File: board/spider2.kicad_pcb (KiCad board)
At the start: 2 copper layers, 137 x 72.5 mm, 143 parts, among them J1 NRJ6HH, J10 PJ-320A, J11 PJ359, J12 PJ359, J13 PJ359, J14 PJ359, J15 PJ359, J16 PJ359, J17 A, J19 PJ359, J2 NRJ6HH, J20 PJ359, J3 PJ359, J4 PJ359, J5 PJ359, J6 PJ-320A, J7 PJ359, J8 PJ359, J9 PJ359, P1 USB4085, Q1 AOI4286, Q2 BC547, Q3 BC547, SW2 200MDP1T2B2M2, SW3 200MDP1T2B2M2, SW4 200MDP3T1B1M6QE, U2 AP63203, U4 NE5532, U5 MAX4062, U6 MAX4062, U7 PAM8406D

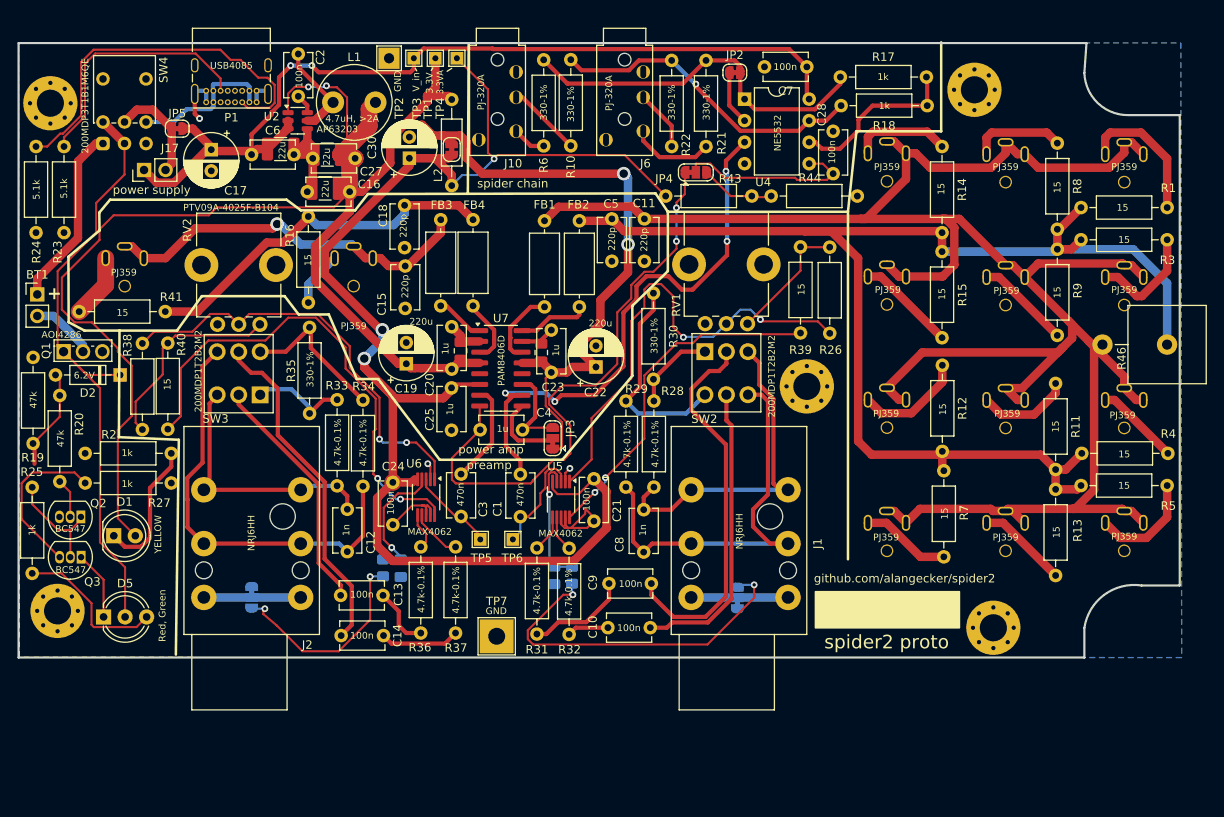
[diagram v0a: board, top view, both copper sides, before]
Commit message: option for poti inversion and some missing connections
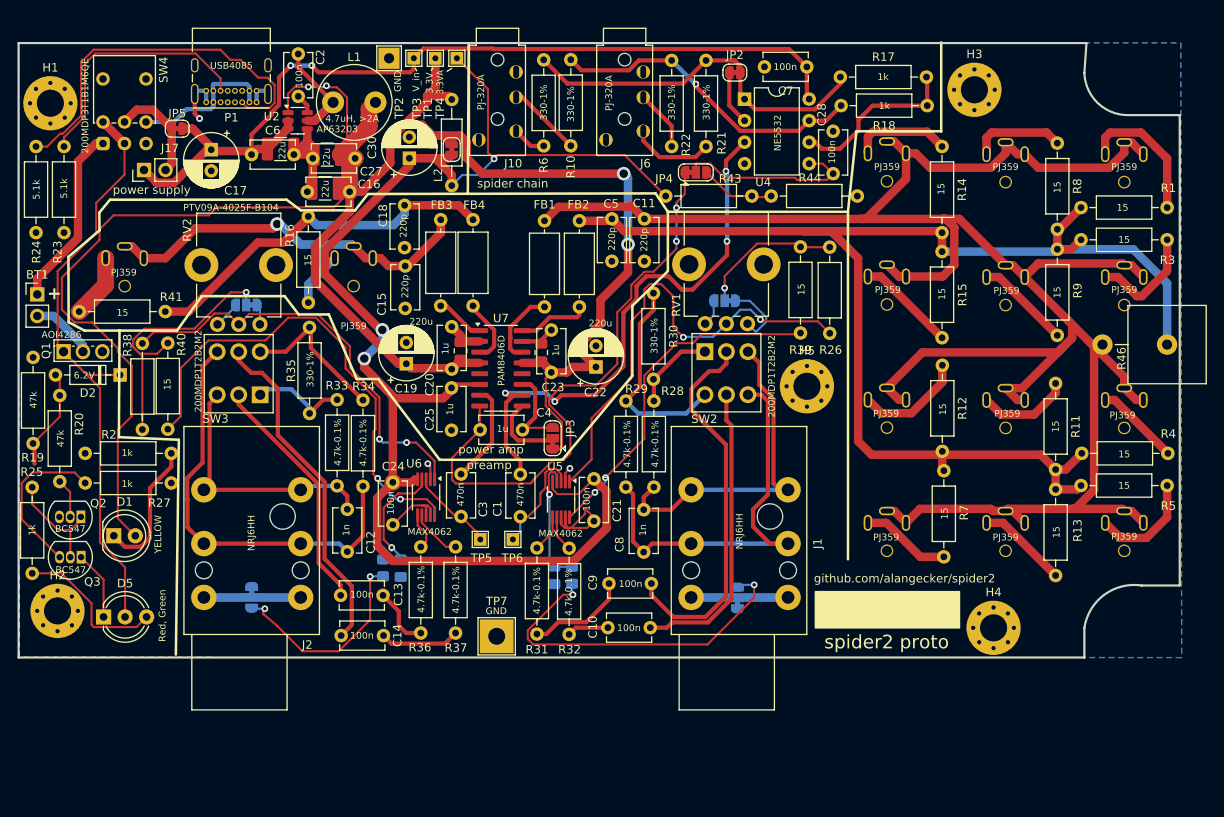
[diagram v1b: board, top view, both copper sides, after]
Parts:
- removed REF** (x5): MountingHole_3.2mm_M3_Pad_Via, MountingHole:MountingHole_3.2mm_M3_Pad_Via
- added H1: ~, MountingHole:MountingHole_3.2mm_M3_Pad_Via, F.Cu at (141.4, 37.7)
- added H2: ~, MountingHole:MountingHole_3.2mm_M3_Pad_Via, F.Cu at (142.2, 97.6)
- added H3: ~, MountingHole:MountingHole_3.2mm_M3_Pad_Via, F.Cu at (250.4, 36.1)
- added H4: ~, MountingHole:MountingHole_3.2mm_M3_Pad_Via, F.Cu at (252.7, 99.6)
- added H5: ~, MountingHole:MountingHole_3.2mm_M3_Pad_Via, F.Cu at (230.7, 71.1)
- added JP8: SolderJumper_3_Bridged12, Jumper:SolderJumper-3_P1.3mm_Bridged12_RoundedPad1.0x1.5mm, B.Cu at (220.9, 61.0)
- added JP9: SolderJumper_3_Bridged12, Jumper:SolderJumper-3_P1.3mm_Bridged12_RoundedPad1.0x1.5mm, B.Cu at (164.5, 61.5)
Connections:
- R26 pad 1: Net-(R26-Pad1) -> Net-(JP8-C)
- R38 pad 1: Net-(R38-Pad1) -> Net-(JP9-C)
- R39 pad 2: Net-(R26-Pad1) -> Net-(JP8-C)
- R40 pad 2: Net-(R38-Pad1) -> Net-(JP9-C)
- RV1 pad 1: Net-(R26-Pad1) -> Net-(JP8-A)
- RV1 pad 3: unconnected-(RV1-Pad3) -> Net-(JP8-B)
- RV2 pad 1: Net-(R38-Pad1) -> Net-(JP9-A)
- RV2 pad 3: unconnected-(RV2-Pad3) -> Net-(JP9-B)
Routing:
- net Net-(JP9-C): track 0.00 -> 32.9 mm, vias 0 -> 1
- net Net-(R38-Pad1): track 23.9 -> 0.00 mm
- net Net-(JP8-C): track 0.00 -> 17.1 mm, vias 0 -> 1
- net Net-(R26-Pad1): track 15.1 -> 0.00 mm
- net Net-(JP8-A): track 0.00 -> 7.98 mm
- net Net-(JP8-B): track 0.00 -> 3.11 mm
- net Net-(JP9-B): track 0.00 -> 2.92 mm
- net Net-(JP9-A): track 0.00 -> 2.16 mm

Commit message: hybrid footprints for 3.5mm jacks
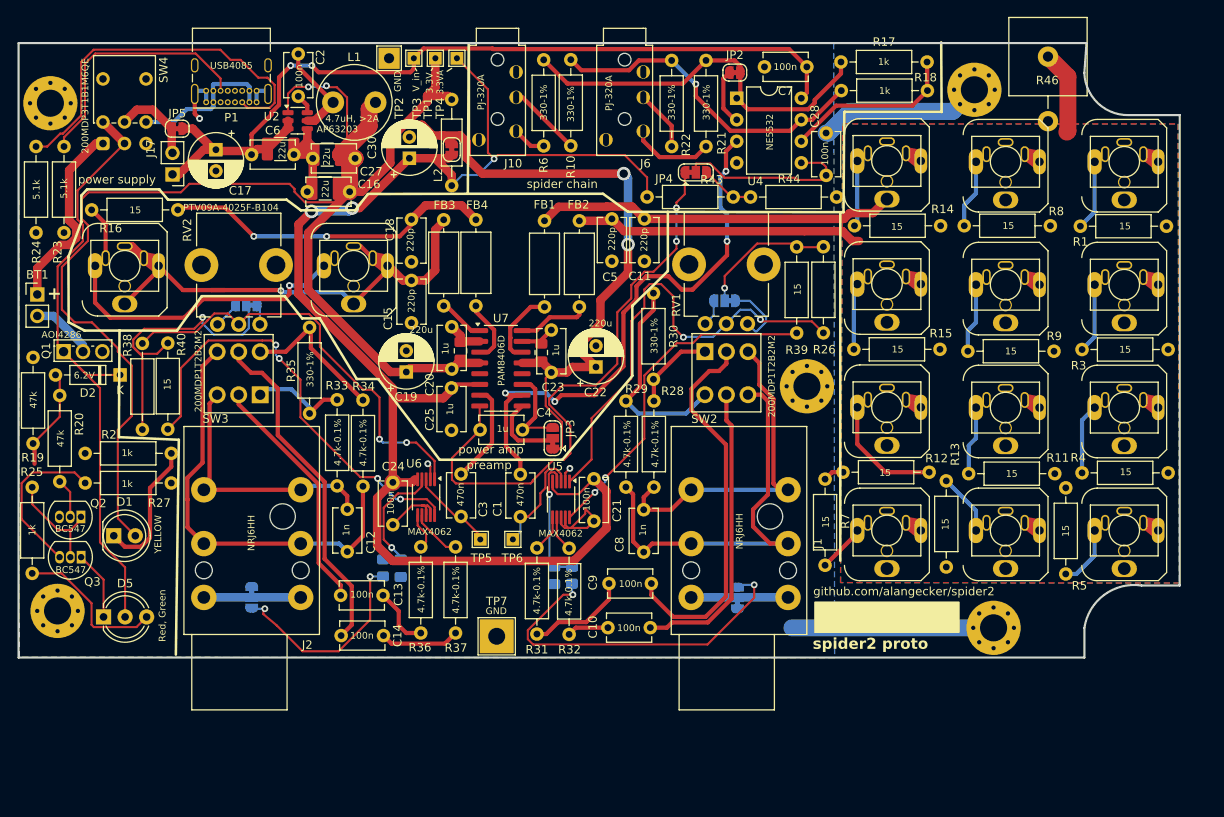
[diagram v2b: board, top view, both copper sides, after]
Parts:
- removed R41: 15, Resistor_THT:R_Axial_DIN0207_L6.3mm_D2.5mm_P10.16mm_Horizontal
- J11, J12, J13, J14, J15, J16, J19, J20, J3, J4, J5, J7, J8, J9: footprint custom:Jack_3.5mm_PJ359 -> custom:Jack_3.5mm_Hybrid_PJ359_20-1655
- moved R46 36.8 mm to (259.1, 32.2), turned to -90 degrees
- moved R16 18.9 mm to (156.4, 50.3), turned to 180 degrees
- moved R13 17.1 mm to (247.1, 82.2), turned to -90 degrees
- moved R3 16.4 mm to (263.1, 66.8), turned to 0 degrees
- moved R5 15.9 mm to (261.2, 93.2), turned to 90 degrees
- moved R11 14.8 mm to (249.7, 81.4), turned to 0 degrees
- moved R8 14.7 mm to (249.2, 52.1), turned to 0 degrees
- moved R7 14.0 mm to (232.8, 92.2)
- moved R14 13.9 mm to (236.3, 52.1), turned to 0 degrees
- moved R12 12.7 mm to (245.1, 81.2), turned to 180 degrees
- moved R9 10.7 mm to (249.6, 67.0), turned to 0 degrees
- moved R15 10.5 mm to (236.2, 66.7), turned to 0 degrees
- moved R1 10.5 mm to (262.9, 52.2), turned to 0 degrees
- moved R4 10.4 mm to (263.1, 81.3), turned to 0 degrees
- moved J17 3.39 mm to (155.8, 46.1), turned to 180 degrees
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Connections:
- J20 pad S: Net-(J20-PadS) -> Net-(J19-PadS)
- R16 pad 1: Net-(J19-PadS) -> Net-(C18-Pad1)
- R16 pad 2: Net-(C18-Pad1) -> Net-(J19-PadS)
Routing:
- net Net-(C5-Pad2): track 258.1 -> 42.7 mm
- net Net-(C11-Pad1): track 156.9 -> 46.6 mm
- net GND: track 65.4 -> 108.8 mm
- net Net-(J19-PadS): track 6.53 -> 41.7 mm, vias 0 -> 1
- net Net-(C15-Pad2): track 44.8 -> 61.8 mm
- net Net-(J3-PadS): track 16.6 -> 8.30 mm
- net +3.3V: track 245.1 -> 253.2 mm
- net Net-(J20-PadS): track 7.60 -> 0.00 mm
- net Net-(U6-G1): track 57.7 -> 51.7 mm, vias 2 -> 4
- net Net-(J7-PadS): track 12.8 -> 7.27 mm
- net Net-(J8-PadS): track 10.6 -> 5.68 mm
- net Net-(J4-PadS): track 13.1 -> 8.26 mm
- net Net-(C18-Pad1): track 43.7 -> 39.3 mm, vias 0 -> 2
- net VCC: track 106.6 -> 102.6 mm
- net Net-(J15-PadS): track 11.7 -> 7.79 mm
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- added copper zone on F.Cu, net Net-(C11-Pad1)
- added copper zone on B.Cu, net Net-(C5-Pad2)
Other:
- board text added: "built by"
- board text added: "originally developed by inspired by spider2 design by with great help of and"
- board text removed: "originally developed by inspired by new board by with great help of and built by"

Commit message: some cleanups
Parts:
- moved R7 0.46 mm to (233.3, 92.2)
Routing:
- net Net-(C11-Pad1): track 46.6 -> 224.1 mm
- net Net-(C5-Pad2): track 42.7 -> 44.7 mm, vias 0 -> 1
- net Net-(J7-PadS): track 7.27 -> 6.54 mm
- removed copper zone on F.Cu, net Net-(C11-Pad1)

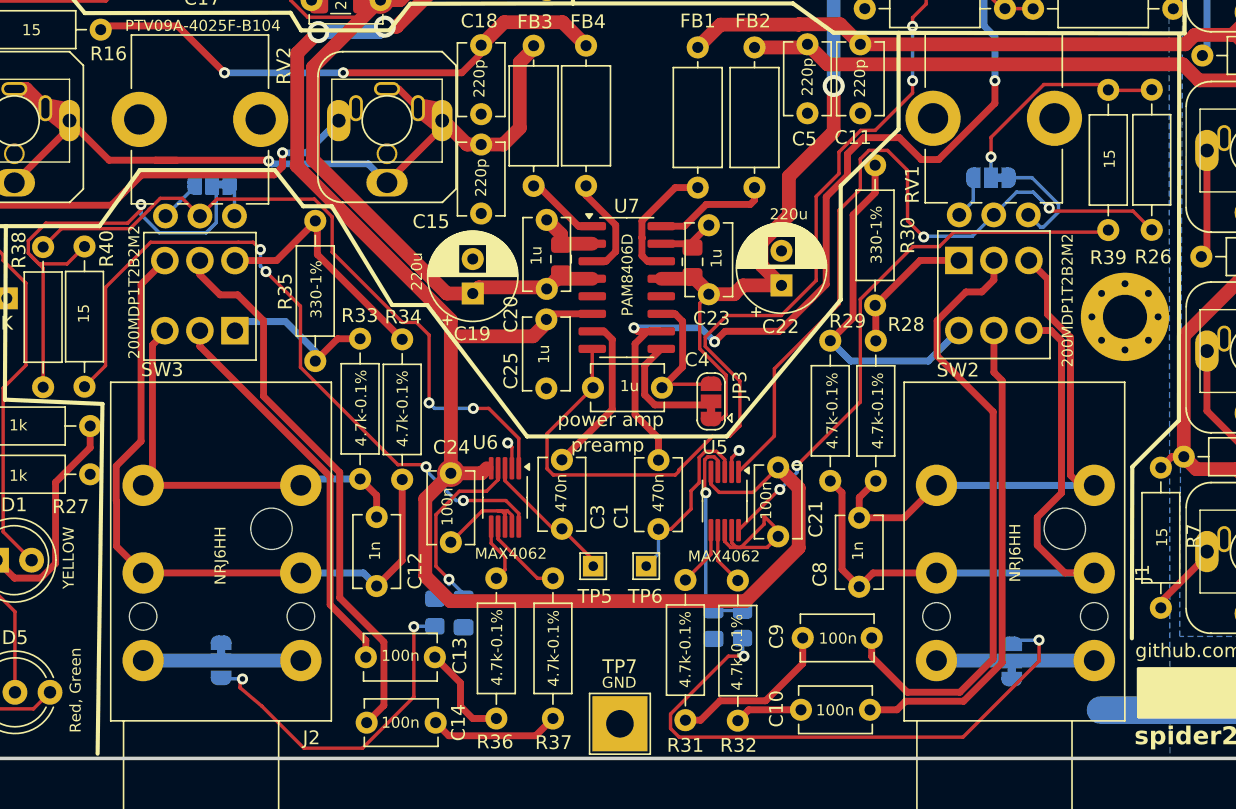
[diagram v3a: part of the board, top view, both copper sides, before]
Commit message: throw out not required pad (-30dB for line signals)
the gain range via poti is sufficient enough for line and mics
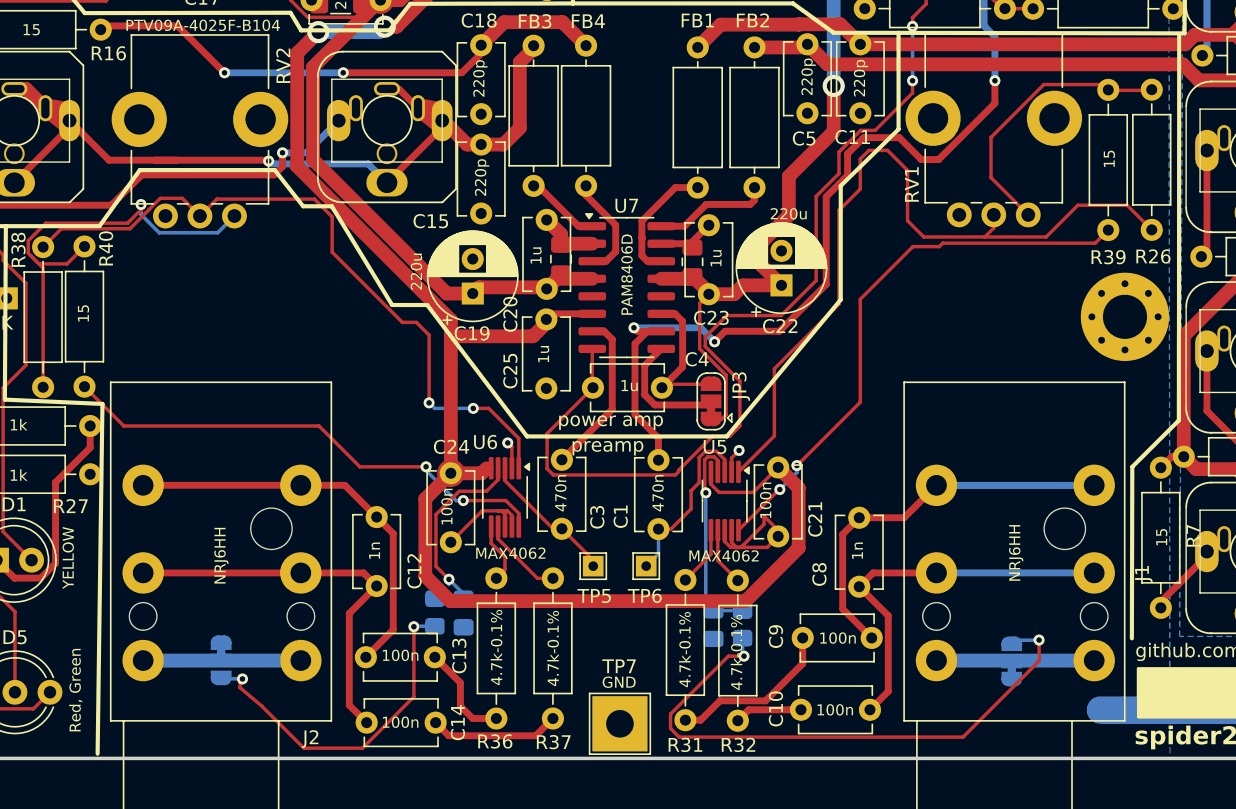
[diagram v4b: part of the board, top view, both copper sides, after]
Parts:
- removed JP8, JP9: SolderJumper_3_Bridged12, Jumper:SolderJumper-3_P1.3mm_Bridged12_RoundedPad1.0x1.5mm
- removed R28, R29, R33, R34: 4.7k-0.1%, Resistor_THT:R_Axial_DIN0207_L6.3mm_D2.5mm_P10.16mm_Horizontal
- removed R30, R35: 330-1%, Resistor_THT:R_Axial_DIN0207_L6.3mm_D2.5mm_P10.16mm_Horizontal
- removed SW2, SW3: 200MDP1T2B2M2, custom:SW_PUSH_E-Switch_200MDPxTxBxM2
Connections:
- C10 pad 1: Net-(SW2B-B) -> /Preamp Interpreter/IN-
- C13 pad 1: Net-(SW3A-B) -> /Preamp Floor/IN+
- C14 pad 1: Net-(SW3B-B) -> /Preamp Floor/IN-
- C9 pad 1: Net-(SW2A-B) -> /Preamp Interpreter/IN+
- R26 pad 1: Net-(JP8-C) -> Net-(R26-Pad1)
- R38 pad 1: Net-(JP9-C) -> Net-(R38-Pad1)
- R39 pad 2: Net-(JP8-C) -> Net-(R26-Pad1)
- R40 pad 2: Net-(JP9-C) -> Net-(R38-Pad1)
- RV1 pad 1: Net-(JP8-A) -> Net-(R26-Pad1)
- RV1 pad 3: Net-(JP8-B) -> unconnected-(RV1-Pad3)
- RV2 pad 1: Net-(JP9-A) -> Net-(R38-Pad1)
- RV2 pad 3: Net-(JP9-B) -> unconnected-(RV2-Pad3)
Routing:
- net Net-(SW2A-B): track 45.2 -> 0.00 mm
- net Net-(SW3B-B): track 40.3 -> 0.00 mm
- net Net-(SW2B-B): track 35.3 -> 0.00 mm
- net Net-(JP9-C): track 35.1 -> 0.00 mm, vias 1 -> 0
- net Net-(R38-Pad1): track 0.00 -> 33.8 mm, vias 0 -> 1
- net Net-(SW3A-B): track 28.7 -> 0.00 mm
- net Net-(SW2B-A): track 24.9 -> 0.00 mm
- net /Preamp Floor/IN-: track 50.7 -> 28.6 mm
- net /Preamp Interpreter/IN-: track 49.2 -> 27.8 mm
- net Net-(R26-Pad1): track 0.00 -> 20.2 mm
- net Net-(SW3B-A): track 18.2 -> 0.00 mm
- net Net-(JP8-C): track 16.4 -> 0.00 mm, vias 1 -> 0
- net Net-(U6-G1): track 51.7 -> 36.4 mm, vias 4 -> 2
- net /Preamp Interpreter/IN+: track 40.0 -> 28.1 mm
- net Net-(SW3A-A): track 11.6 -> 0.00 mm
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
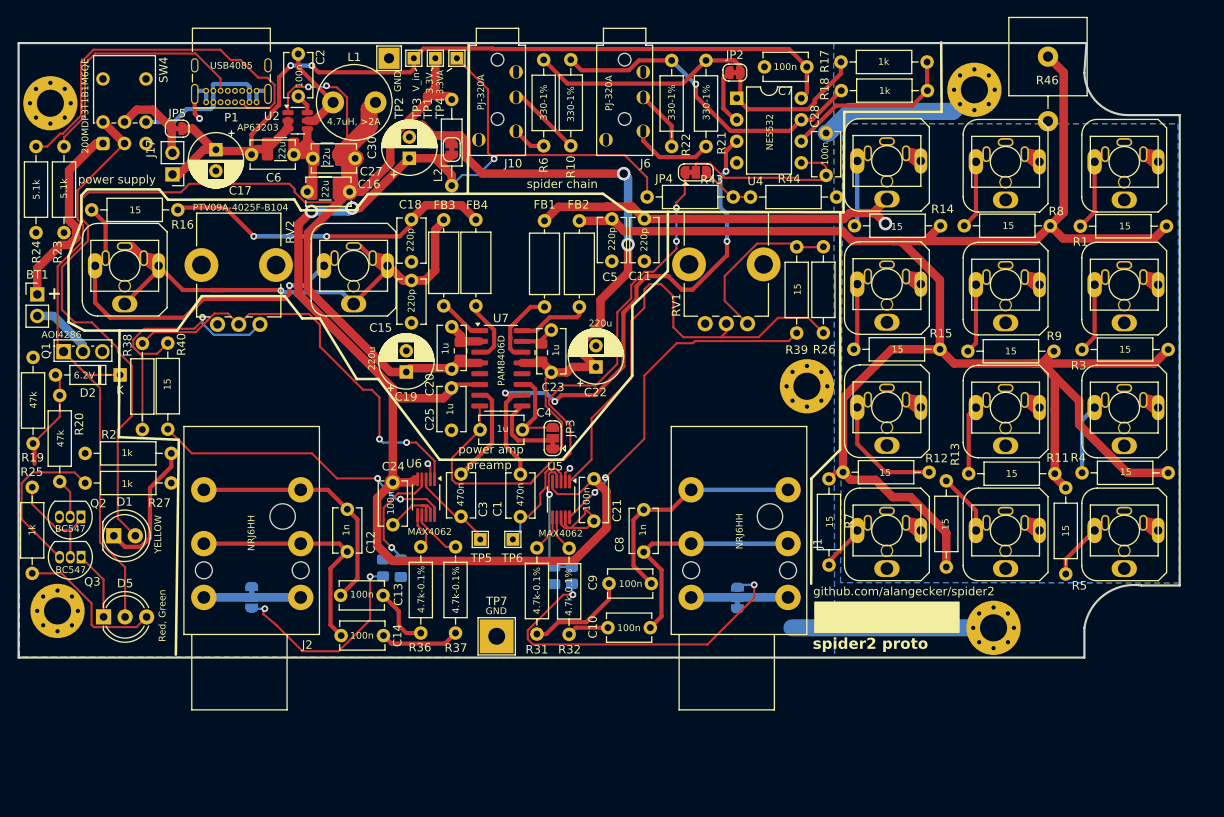
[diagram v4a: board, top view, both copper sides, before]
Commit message: clean up not required components
jumpers, some dnp components, etc.
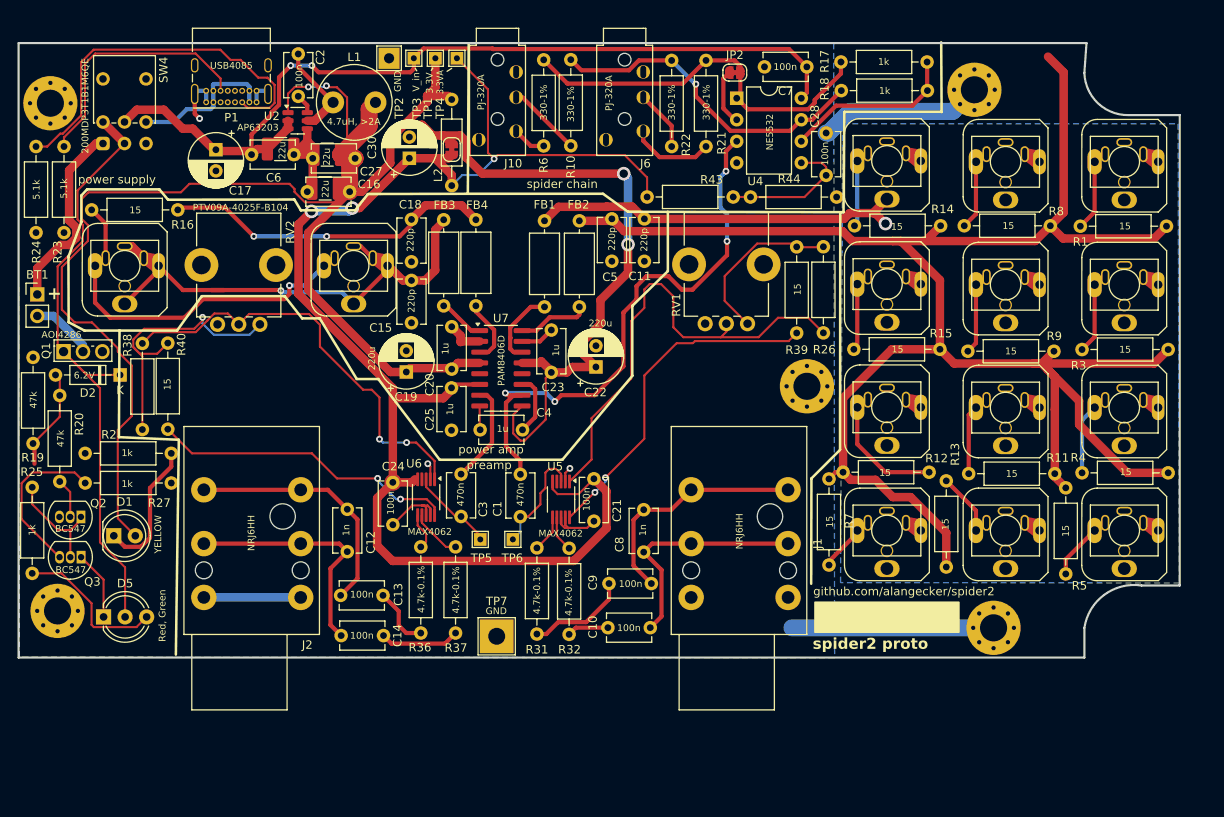
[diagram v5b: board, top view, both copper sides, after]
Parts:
- removed C26, C29: alt, Capacitor_SMD:C_0805_2012Metric_Pad1.18x1.45mm_HandSolder
- removed C31, C32: NC, Capacitor_SMD:C_0805_2012Metric_Pad1.18x1.45mm_HandSolder
- removed J17: A, Connector_PinHeader_2.54mm:PinHeader_1x02_P2.54mm_Vertical
- removed JP3: Mode, Jumper:SolderJumper-3_P1.3mm_Bridged12_RoundedPad1.0x1.5mm
- removed JP4, JP6, JP7: SolderJumper_3_Bridged12, Jumper:SolderJumper-3_P1.3mm_Bridged12_RoundedPad1.0x1.5mm
- removed JP5: Jumper_2_Bridged, Jumper:SolderJumper-2_P1.3mm_Bridged_RoundedPad1.0x1.5mm
- removed R42, R45: NC, Resistor_SMD:R_0805_2012Metric_Pad1.20x1.40mm_HandSolder
- removed R46: NC, Resistor_THT:R_Axial_Power_L25.0mm_W9.0mm_P7.62mm_Vertical
- R43, R44: value NC -> 47k
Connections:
- net VREF renamed Net-(U7-VREF)
- C28 pad 1: Net-(JP4-C) -> Net-(U4B-+)
- J1 pad S: Net-(JP6-C) -> GND
- J1 pad SN: Net-(JP6-C) -> GND
- J2 pad S: Net-(JP7-C) -> GND
- J2 pad SN: Net-(JP7-C) -> GND
- R43 pad 2: Net-(JP4-B) -> Net-(U4B-+)
- R44 pad 1: Net-(JP4-B) -> Net-(U4B-+)
- SW4 pad 5: Net-(J17-Pin_2) -> VCC
- U4 pad 5: Net-(JP4-C) -> Net-(U4B-+)
- U5 pad 4: Net-(U5-BIAS) -> unconnected-(U5-BIAS-Pad4)
- U6 pad 4: Net-(U6-BIAS) -> unconnected-(U6-BIAS-Pad4)
- U7 pad 9: Net-(JP3-C) -> +3.3V
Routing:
- net Net-(U7-VREF): track 69.5 -> 2.84 mm, vias 2 -> 0
- net /Preamp Interpreter/BIAS: track 42.3 -> 0.00 mm, vias 2 -> 0
- net /Preamp Floor/BIAS: track 24.8 -> 0.00 mm, vias 2 -> 0
- net Net-(JP4-C): track 21.5 -> 0.00 mm
- net Net-(U4B-+): track 0.00 -> 16.3 mm
- net Net-(U6-BIAS): track 15.8 -> 0.00 mm, vias 1 -> 0
- net Net-(U5-BIAS): track 15.3 -> 0.00 mm, vias 1 -> 0
- net Net-(JP7-C): track 11.4 -> 0.00 mm
- net Net-(JP6-C): track 11.4 -> 0.00 mm
- net Net-(J17-Pin_2): track 10.00 -> 0.00 mm
- net Net-(JP3-C): track 9.05 -> 0.00 mm
- net Net-(JP4-B): track 6.53 -> 0.00 mm
- net +3.3V: track 253.2 -> 256.9 mm
- net GND: track 108.8 -> 111.7 mm
- net VCC: track 102.6 -> 104.7 mm
